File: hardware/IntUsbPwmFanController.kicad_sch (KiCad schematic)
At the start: 53 parts, among them J1 UsbPortA, J2 UsbPortB, J3 PC power, J6 FAN, J7 USB_Out, J8 GPIO, Q1 IRLML6402, U1 FT260S, U2 AT24CS01-SSHM, U3 ATtiny202-SS

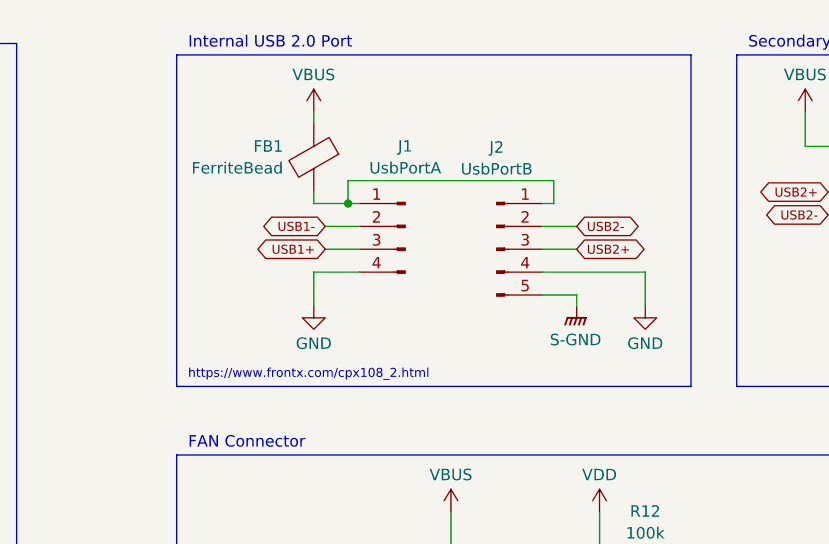
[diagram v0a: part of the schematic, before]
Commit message: Use correct symbol/footprint for the USB 2.0 header
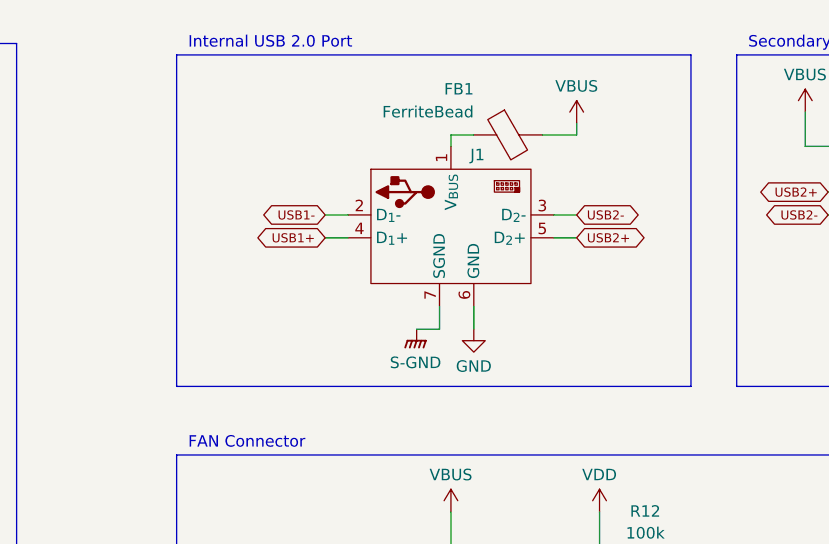
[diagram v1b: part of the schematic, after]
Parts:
- removed J1: UsbPortA, Connector_PinHeader_2.00mm:PinHeader_1x04_P2.00mm_Vertical, symbol Connector:Conn_01x04_Pin
- removed J2: UsbPortB, Connector_PinHeader_2.00mm:PinHeader_1x05_P2.00mm_Vertical, symbol Connector:Conn_01x05_Pin
- added J1: ~, symbol USB:Internal USB 2.0 Connector
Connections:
- net GND: now also J1.6 (GND)
- net S-GND: now also J1.7 (SGND)
- net USB1+: now also J1.4 (D_{1}+)
- net USB1-: now also J1.2 (D_{1}-)
- net USB2+: now also J1.5 (D_{2}+)
- net USB2-: now also J1.3 (D_{2}-)
- net VBUS: now also FB1.2; no longer FB1.1
- new net: FB1.1, J1.1 (V_{BUS})
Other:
- note removed: "https://www.frontx.com/cpx108_2.html"
- moved on the sheet: FB1

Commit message: Add a PCB layout draft
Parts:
- added JP4: INT, Jumper:SolderJumper-2_P1.3mm_Bridged_RoundedPad1.0x1.5mm, symbol Jumper:SolderJumper_2_Bridged
- added TP4: INT, TestPoint:TestPoint_Pad_D1.0mm, symbol Connector:TestPoint
- J1: footprint (none) -> USB:Internal USB 2.0 Pinheader
- J7: now not fitted; now left out of the parts list
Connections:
- net GND: now also D6.1 (K), D7.1 (K), JP4.2 (B); no longer R23.1, R9.1, U1.19 (DIO8/INTRIN)
- net VBUS: no longer J7.1 (VBUS)
- net at R9.2: now also U1.4 (DIO13/GPIOH/DSRN); no longer D6.1 (K)
- net VUSB: now reaches FB1.1, J1.1 (V_{BUS})
- net VUSB: now also J7.1 (VBUS)
- net at R23.2: now also U1.11 (DIO0/TX_ACT); no longer D7.1 (K)
- net at D7.2 (A): now also R23.1; no longer U1.11 (DIO0/TX_ACT)
- net at D6.2 (A): now also R9.1; no longer U1.4 (DIO13/GPIOH/DSRN)
- new net: JP4.1 (A), TP4.1, U1.19 (DIO8/INTRIN)
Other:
- moved on the sheet: D6, D7, R23, R9

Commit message: Adjust schematic and PCB to the new footprint
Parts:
- J1: footprint USB:Internal USB 2.0 Pinheader -> USB:Internal USB 2.0 Socket Default
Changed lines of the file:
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@@
 			)
 		)
-		(property "Footprint" "USB:Internal USB 2.0 Pinheader"
+		(property "Footprint" "USB:Internal USB 2.0 Socket Default"
 			(at 212.09 34.29 0)
 			(effects

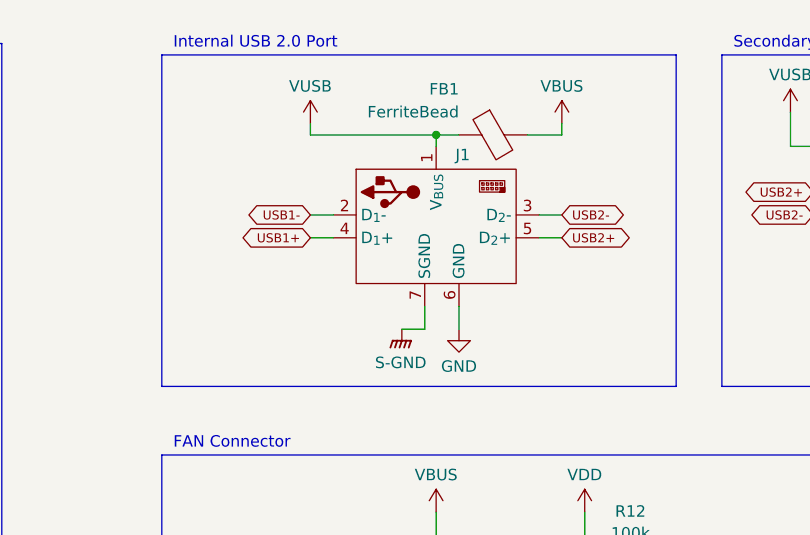
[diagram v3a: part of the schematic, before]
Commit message: Switch to a pinheader for the USB connector
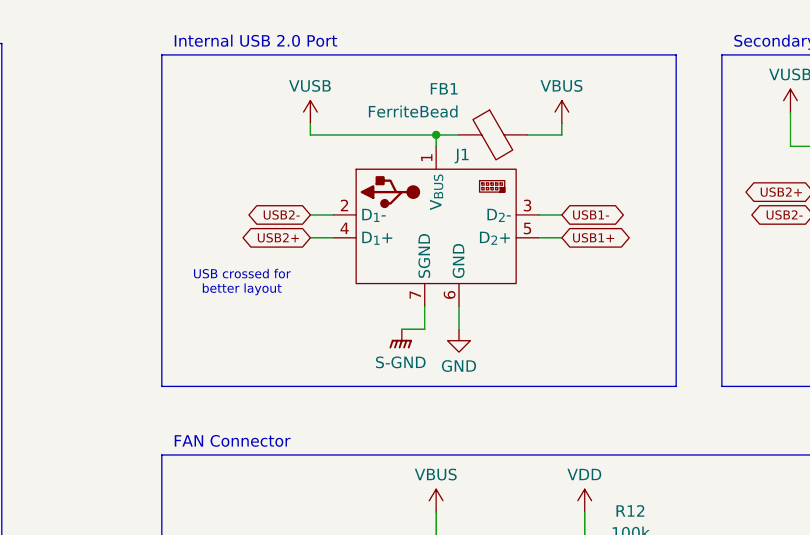
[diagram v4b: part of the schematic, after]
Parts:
- J1: footprint USB:Internal USB 2.0 Socket Default -> USB:Internal USB 2.0 Header Default
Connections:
- net USB1+: now also J1.5 (D_{2}+); no longer J1.4 (D_{1}+)
- net USB1-: now also J1.3 (D_{2}-); no longer J1.2 (D_{1}-)
- net USB2+: now also J1.4 (D_{1}+); no longer J1.5 (D_{2}+)
- net USB2-: now also J1.2 (D_{1}-); no longer J1.3 (D_{2}-)
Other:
- note added: "USB crossed for better layout"
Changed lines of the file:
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@@
 		)
 	)
+	(text "USB crossed for \nbetter layout"
+		(exclude_from_sim no)
+		(at 190.5 44.45 0)
+		(effects
+			(font
+				(size 1 1)
+			)
+		)
+	)
 	(text "EEPROM is not needed\nwith default configiration"
 		(exclude_from_sim no)
@@
 	(global_label "USB2-"
 		(shape bidirectional)
-		(at 226.06 36.83 0)
+		(at 198.12 36.83 180)
 		(fields_autoplaced yes)
 		(effects
@@
 				(size 1 1)
 			)
-			(justify left)
+			(justify right)
 		)
 		(property "Intersheetrefs" "${INTERSHEET_REFS}"
-			(at 234.4758 36.83 0)
+			(at 189.7042 36.83 0)
 			(effects
 				(font
 					(size 1.27 1.27)
 				)
-				(justify left)
+				(justify right)
 				(hide yes)
 			)
@@
 	(global_label "USB2+"
 		(shape bidirectional)
-		(at 226.06 39.37 0)
+		(at 198.12 39.37 180)
 		(fields_autoplaced yes)
 		(effects
@@
 				(size 1 1)
 			)
-			(justify left)
+			(justify right)
 		)
 		(property "Intersheetrefs" "${INTERSHEET_REFS}"
-			(at 234.4758 39.37 0)
+			(at 189.7042 39.37 0)
 			(effects
 				(font
 					(size 1.27 1.27)
 				)
-				(justify left)
+				(justify right)
 				(hide yes)
 			)
@@
 	(global_label "USB1+"
 		(shape bidirectional)
-		(at 198.12 39.37 180)
+		(at 226.06 39.37 0)
 		(fields_autoplaced yes)
 		(effects
@@
 				(size 1 1)
 			)
-			(justify right)
+			(justify left)
 		)
 		(property "Intersheetrefs" "${INTERSHEET_REFS}"
-			(at 189.7042 39.37 0)
+			(at 234.4758 39.37 0)
 			(effects
 				(font
 					(size 1.27 1.27)
 				)
-				(justify right)
+				(justify left)
 				(hide yes)
 			)
@@
 	(global_label "USB1-"
 		(shape bidirectional)
-		(at 198.12 36.83 180)
+		(at 226.06 36.83 0)
 		(fields_autoplaced yes)
 		(effects
@@
 				(size 1 1)
 			)
-			(justify right)
+			(justify left)
 		)
 		(property "Intersheetrefs" "${INTERSHEET_REFS}"
-			(at 189.7042 36.83 0)
+			(at 234.4758 36.83 0)
 			(effects
 				(font
 					(size 1.27 1.27)
 				)
-				(justify right)
+				(justify left)
 				(hide yes)
 			)
@@
 			)
 		)
-		(property "Footprint" "USB:Internal USB 2.0 Socket Default"
+		(property "Footprint" "USB:Internal USB 2.0 Header Default"
 			(at 212.09 34.29 0)
 			(effects
